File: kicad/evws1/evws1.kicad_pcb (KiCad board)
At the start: 4 copper layers, 112 x 144 mm, 301 parts, among them J1 Screw_Terminal_01x03, J10 Screw_Terminal_01x04, J11 USB 2.0 Mini, J12 USB 2.0 Mini, J13 atmega-isp-6, J14 header, J15 Jumper, J16 header, J17 header, J18 header, J19 header, J2 Screw_Terminal_01x02, J20 header, J21 header, J22 header, J23 header, J24 header, J25 header, J26 header, J27 header, J28 header, J3 HB9500-2P, J4 HB9500-3P, J5 Screw_Terminal_01x04, J6 Screw_Terminal_01x03, J7 Screw_Terminal_01x02, J8 HB9500-2P, J9 HB9500-3P, K1 G3MB-202P, K2 G3MB-202P, M1 HLK-PM01, M2 dc-dc-buck-converter-5v-to-3.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, M3 dc-dc-converter-5v-to-p12v-m1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, M5 rpi-ev-plc-adapter-v1.0, Q1 AO3401, Q2 AO3401, Q3 AO3400, Q4 AO3400, Q5 AO3401, Q6 AO3401, Q7 AO3400, SW1 SW_SS13F06-G5, SW2 SW_SS13F06-G5, SW3 SW_Push, SW4 dip-switch-4x2pos-smd-1.27mm, SW5 SS-12D00G3, SW6 SS-12D00G3, SW7 SS-12D00G3, SW8 dip-switch-4x2pos-smd-1.27mm, T1 ZMPT101B, T2 ZMPT101B, U1 atmega324p-20au, U10 max485esa, U11 PC817C, U12 LM258, U13 LM224, U14 LM258, U15 AD633AR, U2 ACS712-30, U3 ACS712-30, U4 PCF8591, U5 ch340g, U6 ch340g, U7 DS1307ZN, U8 24LC512, U9 PCF8574, Y1 20MHz, Y2 12MHz, Y3 12MHz, Y4 32768kHz

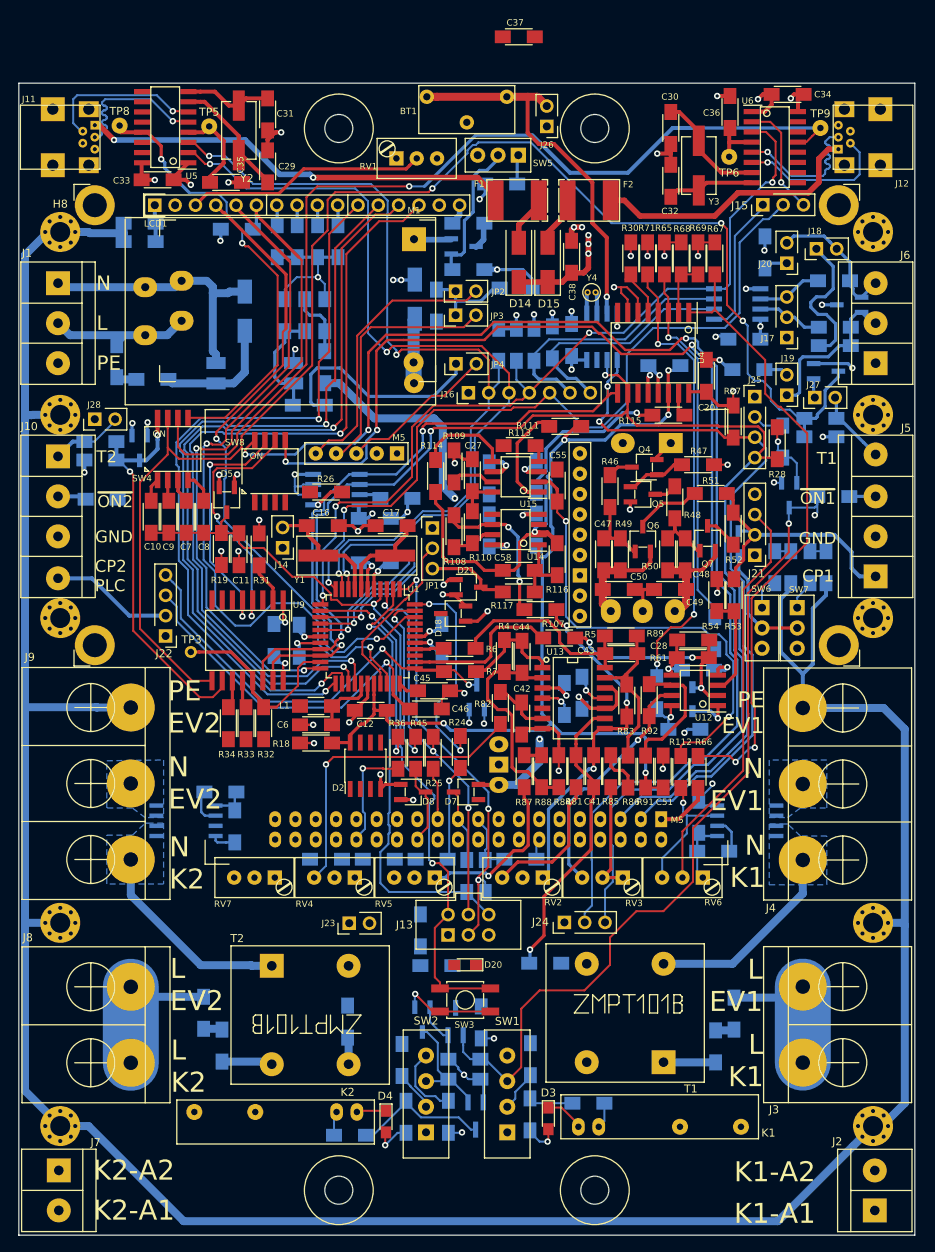
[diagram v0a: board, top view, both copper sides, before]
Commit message: first routing finished, clean DRC
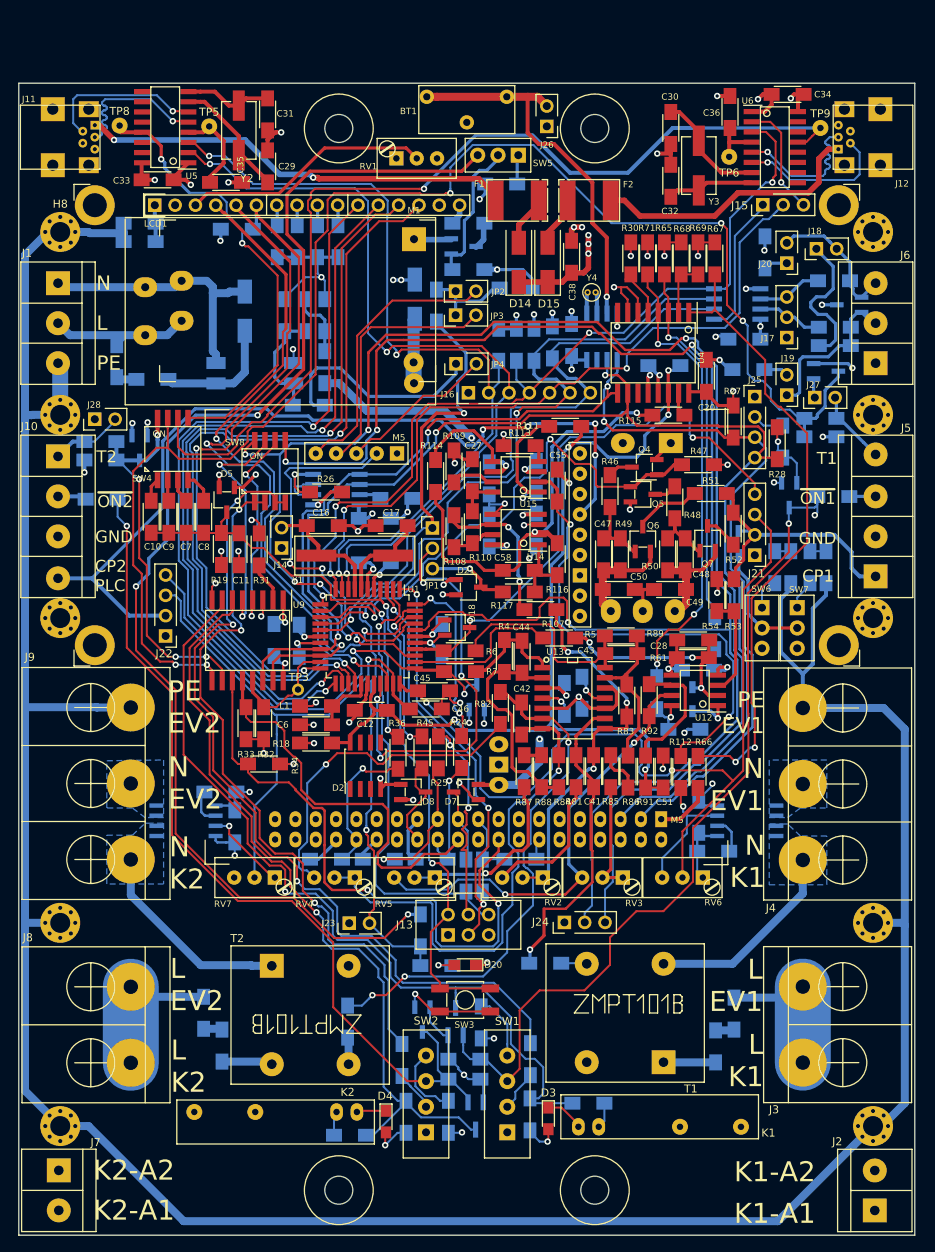
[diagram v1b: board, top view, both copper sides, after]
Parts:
- removed C37: 100n, Project:c-1206-hand-soldering
- moved TP3 14.2 mm to (72.9, 116.8)
- moved R34 6.77 mm to (68.7, 126.1), turned to 0 degrees
- moved D18 1.82 mm to (92.8, 109.0), turned to 0 degrees
- moved R45 0.80 mm to (88.4, 124.7)
- moved R25 0.65 mm to (90.5, 124.7)
- moved R35 0.35 mm to (96.0, 140.1)
- moved R6 0.30 mm to (93.1, 112.0)
- moved Y1 0.25 mm to (80.0, 100.0)
- moved R24 0.15 mm to (93.3, 124.6)
- moved J14 0.13 mm to (70.8, 99.1)
- moved R44 0.11 mm to (93.9, 140.1)
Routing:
- net Net-(R102-Pad2): track 0.00 -> 159.1 mm, vias 0 -> 3
- net /Microcontroller/~K1-ON: track 0.00 -> 107.7 mm, vias 0 -> 3
- net /Microcontroller/DEBUG: track 0.00 -> 99.8 mm, vias 0 -> 2
- net /Microcontroller/K1-IS-ON: track 5.55 -> 104.0 mm, vias 0 -> 1
- net /~EV2: track 14.6 -> 108.7 mm, vias 0 -> 1
- net /CP2: track 15.4 -> 107.6 mm, vias 0 -> 4
- net /Microcontroller/~K2-ON: track 0.00 -> 89.1 mm, vias 0 -> 3
- net /Microcontroller/K2-IS-ON: track 17.0 -> 96.9 mm, vias 0 -> 1
- net /Microcontroller/RECONNECT: track 3.51 -> 76.5 mm, vias 0 -> 2
- net /AD-V1: track 3.64 -> 70.0 mm, vias 0 -> 2
- net Net-(C42-Pad1): track 6.94 -> 65.2 mm, vias 0 -> 3
- net /AD-I1: track 53.5 -> 111.4 mm, vias 0 -> 2
- net GND: track 254.3 -> 309.6 mm, vias 54 -> 65
- net Net-(C42-Pad2): track 10.5 -> 65.5 mm
- net /Microcontroller/AD-VC2: track 0.00 -> 47.5 mm, vias 0 -> 3
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
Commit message: ...
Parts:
- added J29: header, Project:idc-header-1x02-p2.54mm-vertical, F.Cu at (83.9, 46.2)
- C35: value 100n -> 1n; moved to B.Cu
- C5: value 1n -> 100n; moved to F.Cu
- moved C5 76.6 mm to (62.0, 53.0), turned to 0 degrees
- moved C35 76.2 mm to (63.2, 129.6), turned to 180 degrees
- moved TP5 22.3 mm to (83.9, 49.6)
- moved SW5 19.5 mm to (117.2, 47.0), turned to 90 degrees
- moved R22 18.9 mm to (117.2, 54.5), turned to 90 degrees
- moved RV1 15.6 mm to (70.6, 44.9), turned to 180 degrees
- moved R28 5.74 mm to (127.3, 87.8), turned to 90 degrees
- moved TP6 5.30 mm to (126.6, 44.9)
- moved Y3 2.80 mm to (125.8, 51.4)
- moved C29 2.67 mm to (66.5, 51.0)
- moved C36 2.67 mm to (125.2, 42.5), turned to 180 degrees
- moved C31 2.66 mm to (66.5, 44.6)
- moved Y2 2.64 mm to (62.9, 46.5)
- moved C4 2.63 mm to (122.1, 47.0)
- moved C32 2.62 mm to (122.1, 53.5)
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- renumbered C4 to C30, C30 to C4, J25 to J15, J15 to JP5, J18 to JP6, J19 to JP7, J20 to JP8, K1 to SSR1, K2 to SSR2, J16 to T1, J21 to T2, J17 to T3, J22 to T4, J23 to T5, J24 to T6, T1 to TR1, T2 to TR2
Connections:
- C35 pad 1: Net-(C35-Pad1) -> GND
- C35 pad 2: GND -> Net-(C35-Pad2)
- C5 pad 1: GND -> Net-(C5-Pad1)
- C5 pad 2: Net-(C5-Pad2) -> GND
- TP5 pad 1: Net-(C35-Pad1) -> Net-(C5-Pad1)
- U3 pad 6: Net-(C5-Pad2) -> Net-(C35-Pad2)
- U5 pad 4: Net-(C35-Pad1) -> Net-(C5-Pad1)
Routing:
- net Net-(C5-Pad1): track 0.00 -> 34.0 mm, vias 0 -> 1
- net Net-(Q3-Pad1): track 18.0 -> 51.7 mm
- net Net-(R102-Pad2): track 159.1 -> 183.5 mm, vias 3 -> 4
- net Net-(C35-Pad1): track 11.7 -> 0.00 mm
- net Net-(LCD1-Pad3): track 31.2 -> 19.5 mm
- net GND: track 309.6 -> 318.8 mm, vias 65 -> 64
- net /EV1X: track 188.7 -> 181.5 mm
- net /Microcontroller/UC-TXD0: track 104.5 -> 111.5 mm
- net /Microcontroller/UC-RXD0: track 100.7 -> 107.0 mm
- net Net-(C5-Pad2): track 4.66 -> 0.00 mm
- net Net-(C35-Pad2): track 0.00 -> 4.66 mm
- net /Microcontroller/SCL: track 168.2 -> 172.2 mm
- net /Microcontroller/~RESET2: track 122.9 -> 119.4 mm
- net PE: track 410.5 -> 407.4 mm
- net /Microcontroller/RECONNECT: track 76.5 -> 79.6 mm
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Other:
- board text added: "(LCD)"
- board text added: "+"
- board text added: "+5V"
- board text added: "-"
- board text added: "12MHz"
- board text added: "32768kHz"
- board text added: "3V (BAT)"
- board text added: "3V3"
- board text added: "5V"
- board text added: "A"
- board text added: "A-PU"
- board text added: "B"
- board text added: "B-PD"
- board text added: "CHG"
- board text added: "CONNECTED"
- board text added: "CONNECTING"
- board text added: "CONTROL"
- board text added: "CTRL"
- board text added: "D4"
- board text added: "D5"
- board text added: "D6"
- board text added: "D7"
- board text added: "DE1"
- board text added: "DEBUG"
- board text added: "DEBUG (PA7)"
- board text added: "E"
- board text added: "EV1"
- board text added: "EV2"
- board text added: "I1"
- board text added: "I1-GAIN"
- board text added: "I2"
- board text added: "I2-GAIN"
- board text added: "K"
- board text added: "LCD CONTRAST"
- board text added: "LCD ON"
- board text added: "MISO"
- board text added: "MODB"
- board text added: "MODBUS"
- board text added: "OFF"
- board text added: "ON"
- board text added: "PB0"
- board text added: "PB1"
- board text added: "PLUGIN"
- board text added: "RESET"
- board text added: "RS"
- board text added: "RS485"
- board text added: "RTC CR2025 3V"
- board text added: "RW"
- board text added: "RX0"
- board text added: "RX1"
- board text added: "SCL"
- board text added: "SDA"
- board text added: "SIMULATE"
- board text added: "TERM"
- board text added: "TX0"
- board text added: "TX1"
- board text added: "UART0"
- board text added: "UART0 3V3"
- board text added: "UART1"
- board text added: "USB"
- board text added: "V1"
- board text added: "V1-GAIN"
- board text added: "V1-OFFS"
- board text added: "V2"
- board text added: "V2-GAIN"
- board text added: "VO"
- board text added: "XTAL1"
- board text added: "ZERO DET"
- board text added: "~DTR"
- board text added: "~RE1"
- board text added: "~RES"
- board text added: "~U1"
- board text added: "~U2"

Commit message: V1.0 Design finished
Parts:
- added JP9: header, Project:idc-header-1x03-p2.54mm-vertical, F.Cu at (82.8, 145.7)
- added R35: 270R, Project:r-1206-hand-soldering, B.Cu at (96.0, 140.1)
- T2: footprint Project:idc-header-1x04-p2.54mm-vertical -> Project:idc-header-1x06-p2.54mm-vertical
- T6: footprint Project:idc-header-1x03-p2.54mm-vertical -> Project:idc-header-1x04-p2.54mm-vertical
- moved R102 19.2 mm to (107.3, 148.3), turned to 180 degrees
- moved T5 8.07 mm to (86.0, 150.5), turned to 180 degrees
- moved R74 4.61 mm to (100.1, 73.7)
- moved R73 4.10 mm to (104.3, 73.7)
- moved R80 3.47 mm to (132.1, 74.9)
- moved LCD2 3.18 mm to (130.1, 77.0)
- moved T6 1.90 mm to (104.3, 145.8)
- moved R95 1.30 mm to (48.2, 87.1)
- moved R97 1.10 mm to (48.2, 89.2)
- moved R27 1.05 mm to (127.2, 80.2)
- moved T2 0.91 mm to (130.1, 100.9)
- moved R28 0.80 mm to (127.4, 87.0)
- moved C30 0.80 mm to (124.8, 137.8)
- moved C35 0.80 mm to (63.2, 128.8)
- moved C40 0.50 mm to (120.7, 121.7)
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- renumbered D19 to D3, D21 to D4, J26 to J15, J27 to J16, J28 to J17, J29 to J18, J15 to LCD2, D20 to LED1, D4 to LED2, D3 to LED3, M5 to M4, TP8 to T10, TP9 to T11, TP3 to T7, TP5 to T8, TP6 to T9
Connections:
- net Net-(J24-Pad2) renamed /Microcontroller/PB0
- D4 pad 3: /Measurement/E1 -> /AD-E1
- JP1 pad 3: /Measurement/E1 -> /AD-E1
- R102 pad 1: /Microcontroller/DEBUG -> /Microcontroller/LCD1-BL
- R103 pad 2: /Microcontroller/DEBUG -> Net-(JP9-Pad2)
- R114 pad 2: Net-(R114-Pad2) -> /AD-P1
- R117 pad 1: /Measurement/E1 -> /AD-E1
- SW8 pad 2: Net-(J24-Pad3) -> /Microcontroller/PB1
- T1 pad 4: /Microcontroller/UC-TXD1 -> /Microcontroller/~RE1
- T1 pad 5: /Microcontroller/UC-RXD1 -> /Microcontroller/DE1
- T1 pad 6: /Microcontroller/DE1 -> /Microcontroller/UC-TXD1
- T1 pad 7: /Microcontroller/~RE1 -> /Microcontroller/UC-RXD1
- T6 pad 3: Net-(J24-Pad3) -> /Microcontroller/LCD1-BL
- U1 pad 41: Net-(J24-Pad3) -> /Microcontroller/PB1
- U15 pad 5: Net-(R114-Pad2) -> /AD-P1
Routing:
- net /Microcontroller/PB1: track 0.00 -> 199.5 mm, vias 0 -> 6
- net Net-(J24-Pad3): track 198.9 -> 0.00 mm, vias 6 -> 0
- net GND: track 318.8 -> 441.5 mm
- net +5V: track 140.7 -> 223.4 mm
- net /AD-E1: track 0.00 -> 72.5 mm, vias 0 -> 3
- net /AD-P1: track 0.00 -> 53.9 mm, vias 0 -> 2
- net /Microcontroller/PB0: track 202.3 -> 239.7 mm, vias 4 -> 5
- net Net-(R102-Pad2): track 183.5 -> 207.8 mm
- net Net-(JP9-Pad2): track 0.00 -> 12.0 mm, vias 0 -> 1
- net Net-(R114-Pad2): track 11.9 -> 0.00 mm
- net /Measurement/E1: track 10.4 -> 0.00 mm, vias 1 -> 0
- net /Microcontroller/UC-TXD1: track 106.9 -> 113.0 mm
- net /Microcontroller/DEBUG: track 99.7 -> 94.6 mm
- net /Microcontroller/DE1: track 85.7 -> 80.7 mm, vias 2 -> 1
- net /Microcontroller/~RE1: track 84.3 -> 79.4 mm, vias 1 -> 3
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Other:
- board text added: "1"
- board text added: "10"
- board text added: "12"
- board text added: "14"
- board text added: "16"
- board text added: "18"
- board text added: "2"
- board text added: "20"
- board text added: "22"
- board text added: "24"
- board text added: "26"
- board text added: "28"
- board text added: "30"
- board text added: "32"
- board text added: "34"
- board text added: "36"
- board text added: "38"
- board text added: "4"
- board text added: "40"
- board text added: "41"
- board text added: "42"
- board text added: "43"
- board text added: "44"
- board text added: "45"
- board text added: "51"
- board text added: "57"
- board text added: "58"
- board text added: "6"
- board text added: "8"
- board text added: "BL"
- board text added: "E1"
- board text added: "Electro Vehicle Wallbox Station 1"
- board text added: "LED"
- board text added: "P1"
- board text added: "P2"
- board text added: "PA7"
- board text added: "PB2"
- board text added: "PLC ZERO DETECTION"
- board text added: "V1.0 / 23.2.2020"
- board text added: "VE1"
- board text added: "https://github.com/greenenergyprojects/electro-vehicle-wallbox-station/evws1/kicad"
- board text added: "~IRQ"
- board text added: "~K1-ON"
- board text added: "~K2-ON"
- board text removed: "(LCD)"
- board text removed: "DEBUG (PA7)"
- board text removed: "ZERO DET"
